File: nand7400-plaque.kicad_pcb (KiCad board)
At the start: 2 copper layers, 100 x 20 mm, 4 parts

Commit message: inverted text/paste
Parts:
- removed the G*** at (140.2, 75.5)
- added G***: LOGO, nand7400-plaque:negative-14seg, F.Cu at (140.3, 77.2)

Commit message: doesn't short the board anymore
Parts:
- moved G*** 0.98 mm to (140.2, 76.2)
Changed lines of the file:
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@@
       (drillshape 0)
       (scaleselection 1)
-      (outputdirectory ""))
+      (outputdirectory "Gerbers/"))
   )
   (net 0 "")
@@
   )
   (module nand7400-plaque:negative-14seg (layer F.Cu)
-    (at 140.325 77.175)
+    (at 140.2 76.2)
     (fp_text reference G*** (at 0 0) (layer F.SilkS) hide
       (effects (font (size 1.524 1.524) (thickness 0.3)))
@@
   (gr_arc (start 95.15 73.35) (end 95.15 68.35) (angle -90) (layer Edge.Cuts) (width 0.05))
   (gr_arc (start 185.15 73.35) (end 190.15 73.35) (angle -90) (layer Edge.Cuts) (width 0.05))
-  (zone (net 0) (net_name "") (layer F.Paste) (hatch edge 0.508)
+  (zone (net 0) (net_name "") (layers F&B.Cu) (hatch edge 0.508)
     (connect_pads (clearance 0.508))
     (min_thickness 0.254)
-    (fill yes (arc_segments 32) (thermal_gap 0.508) (thermal_bridge_width 0.508))
+    (keepout (tracks not_allowed) (vias not_allowed) (copperpour not_allowed))
+    (fill (arc_segments 32) (thermal_gap 0.508) (thermal_bridge_width 0.508))
     (polygon
       (pts
-        (xy 191.125 89.45) (xy 181.85 89.625) (xy 182.025 70.025) (xy 98.975 69.875) (xy 98.725 84.975)
-        (xy 179.325 85.125) (xy 179.2 89.65) (xy 89.15 89.45) (xy 89.55 67.75) (xy 191.125 67.75)
+        (xy 149.675 89.975) (xy 131.075 89.975) (xy 131.075 84.3) (xy 149.675 84.3)
       )
     )
@@
     (polygon
       (pts
-        (xy 182.425 89.95) (xy 177.775 89.6) (xy 178.625 85.3) (xy 182.325 85.2)
+        (xy 191 69.1) (xy 190.725 89.25) (xy 148.65 90) (xy 148.625 84.25) (xy 181.425 84.1)
+        (xy 181.575 67.1) (xy 181.575 67.075)
       )
     )
+  )
+  (zone (net 0) (net_name "") (layer F.Paste) (hatch edge 0.508)
+    (connect_pads (clearance 0.508))
+    (min_thickness 0.254)
+    (fill yes (arc_segments 32) (thermal_gap 0.508) (thermal_bridge_width 0.508))
+    (polygon
+      (pts
+        (xy 98.575 83.675) (xy 131.55 84.2) (xy 131.55 89.9) (xy 89.525 89.9) (xy 89.525 67.4)
+        (xy 98.575 67.25)
+      )
+    )

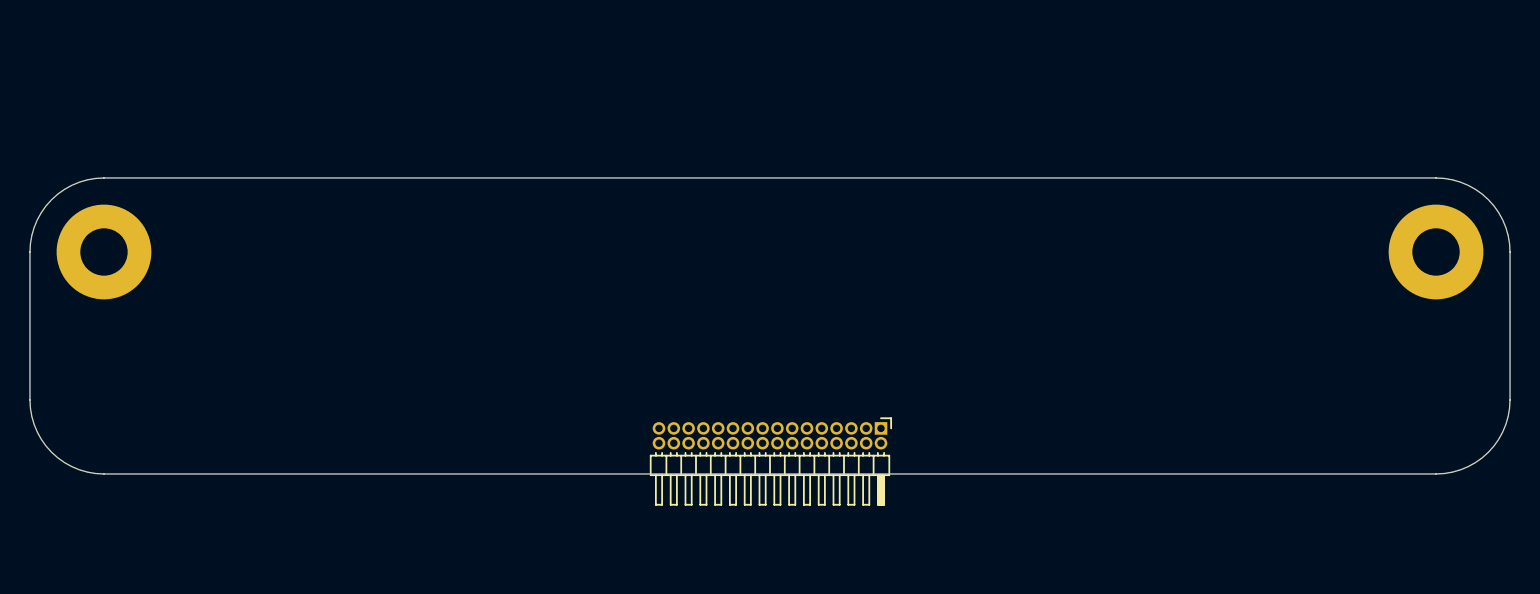
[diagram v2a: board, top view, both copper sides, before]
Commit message: updates to 2.54mm pitch
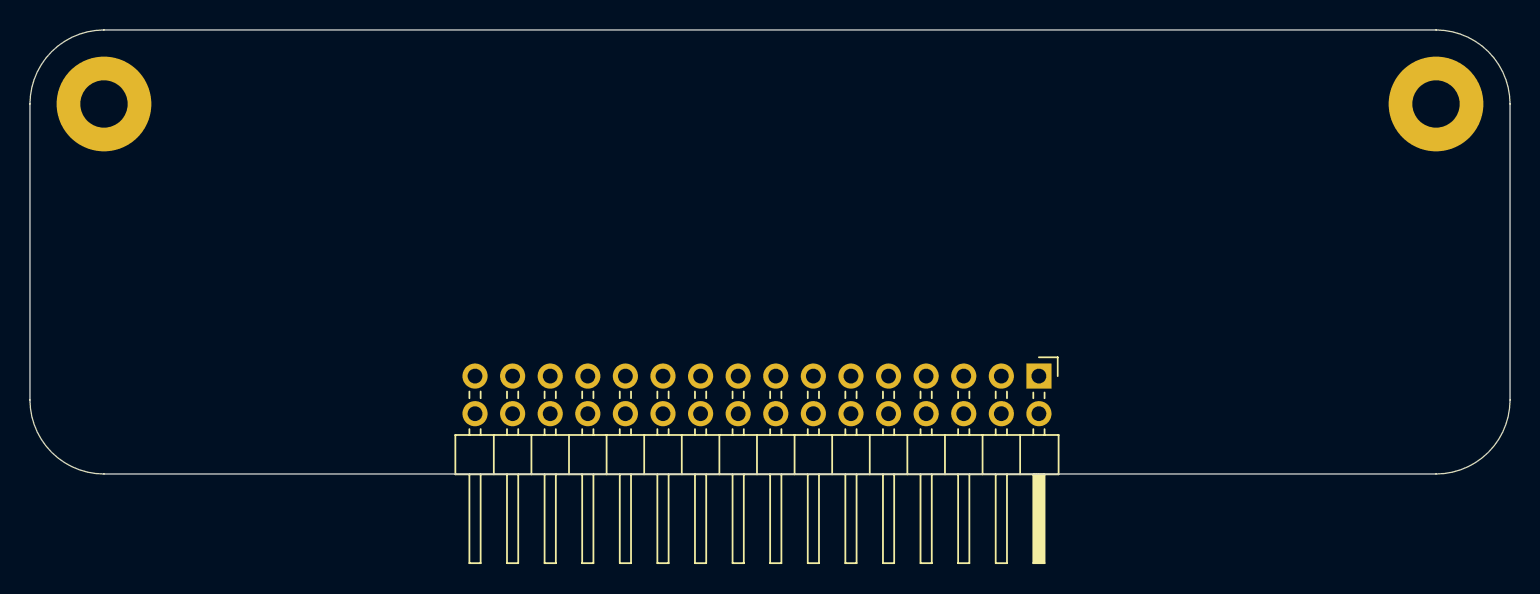
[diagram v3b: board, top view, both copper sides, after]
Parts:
- removed the REF** at (95.2, 73.3)
- removed the REF** at (185.2, 73.3)
- added REF**: MountingHole_3.2mm_M3_Pad, MountingHole:MountingHole_3.2mm_M3_Pad, F.Cu at (95.2, 63.4)
- added REF**: MountingHole_3.2mm_M3_Pad, MountingHole:MountingHole_3.2mm_M3_Pad, F.Cu at (185.2, 63.4)
- REF**: value PinHeader_2x16_P1.00mm_Horizontal -> PinHeader_2x16_P2.54mm_Horizontal; footprint Connector_PinHeader_1.00mm:PinHeader_2x16_P1.00mm_Horizontal -> Connector_PinHeader_2.54mm:PinHeader_2x16_P2.54mm_Horizontal
- moved REF** 11.2 mm to (158.3, 81.7)
- moved G*** 8.75 mm to (140.2, 67.5)
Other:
- board size 100 x 20 mm -> 100 x 30 mm

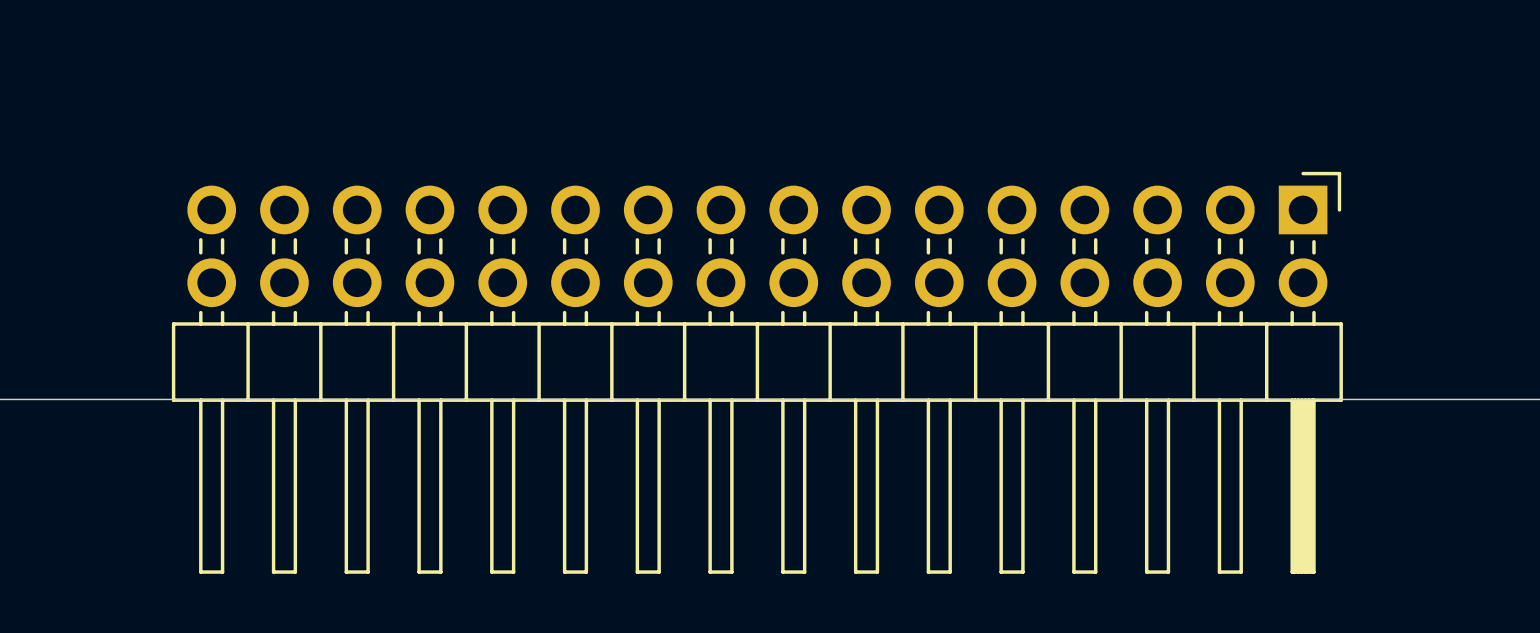
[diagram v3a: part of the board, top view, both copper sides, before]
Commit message: centered 2.54mm header
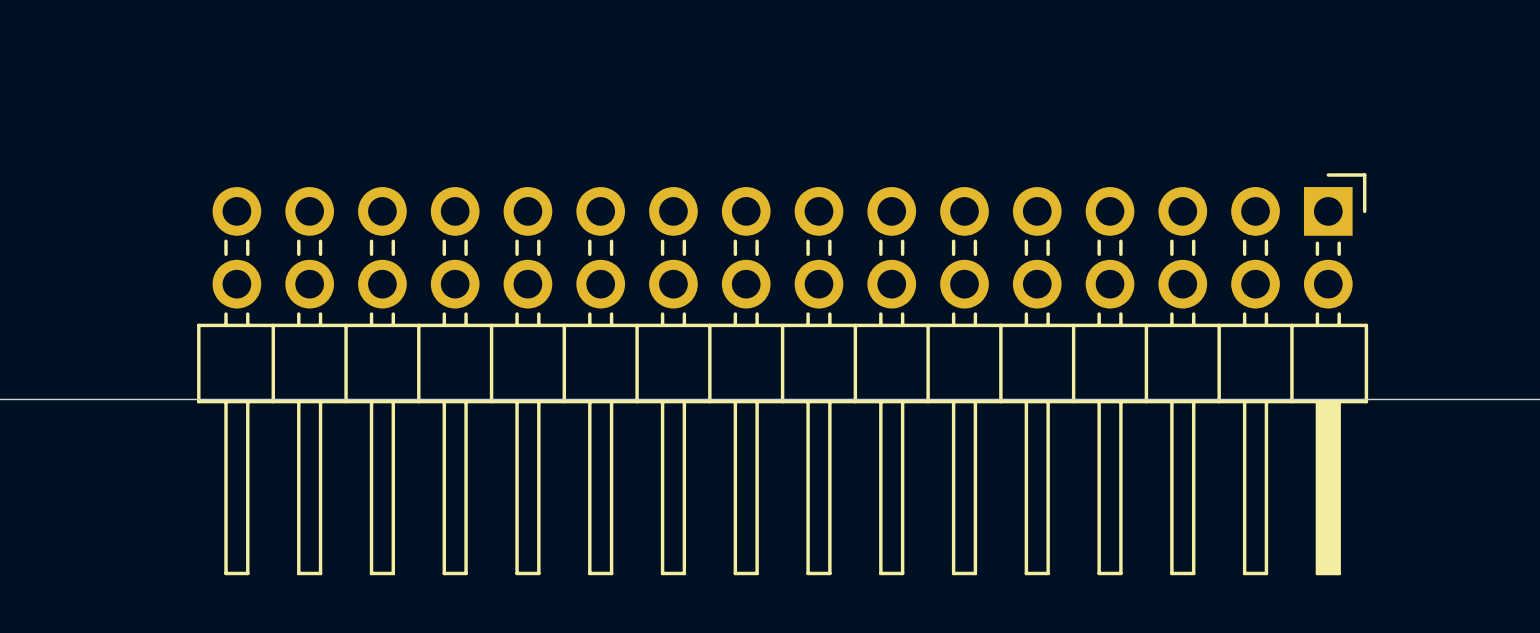
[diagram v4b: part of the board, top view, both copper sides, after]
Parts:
- moved REF** 0.88 mm to (159.2, 81.8)

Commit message: updates
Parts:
- moved G*** 1.72 mm to (140.2, 69.2)

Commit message: rev 2
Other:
- net class Default removed
